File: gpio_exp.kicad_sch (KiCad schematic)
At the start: 17 parts, among them U41 PCA9539AHF

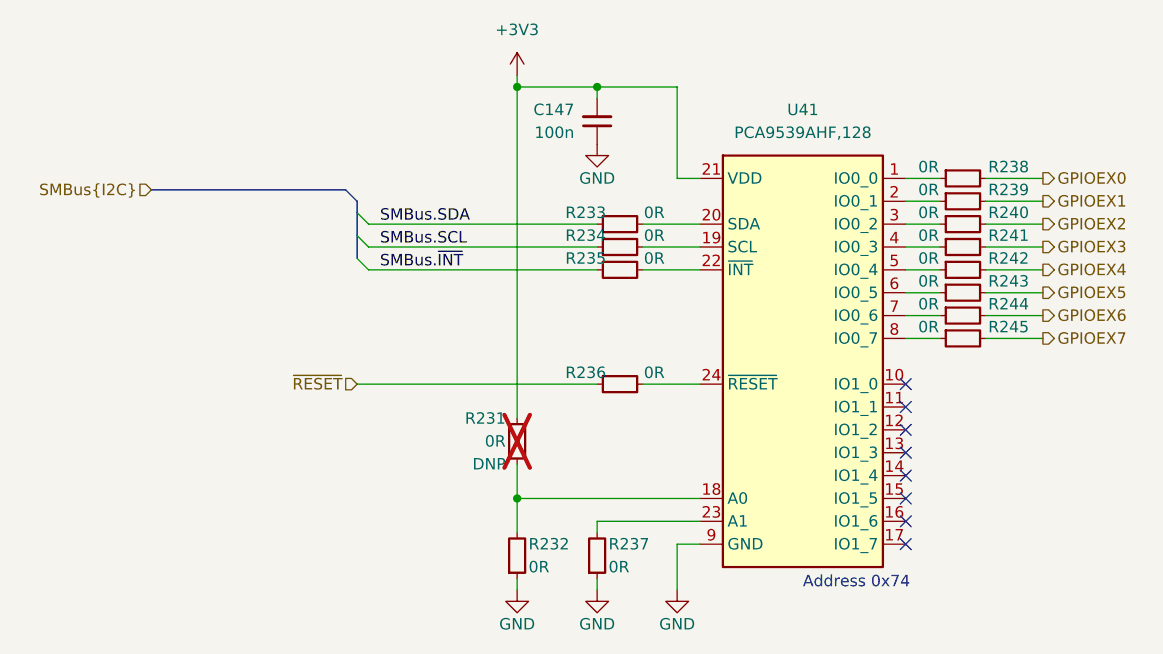
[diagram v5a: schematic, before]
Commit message: Update components from the library
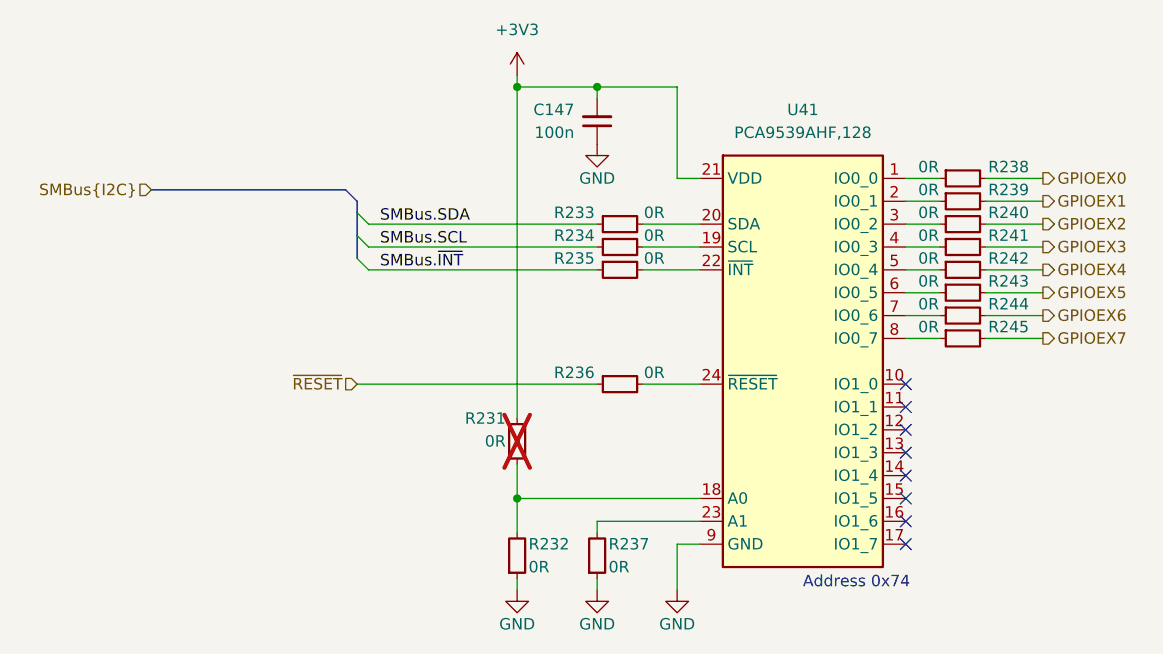
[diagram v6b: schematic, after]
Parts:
- C147, R232, R233, R234, R235, R236, R237, R238, R239, R240, R241, R242, R243, R244, R245: Public (none) -> False
- R231: DNP DNP -> (none); Public (none) -> False
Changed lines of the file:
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@@
       (effects (font (size 1.27 1.27) (thickness 0.15)) (justify left bottom) hide)
+    )
+    (property "Public" "False" (at 247.65 180.34 0)
+      (effects (font (size 1.27 1.27)) (justify left bottom) hide)
     )
     (pin "1")
@@
       (effects (font (size 1.27 1.27) (thickness 0.15)) (justify left bottom) hide)
     )
+    (property "Public" "False" (at 247.65 170.18 0)
+      (effects (font (size 1.27 1.27)) (justify left bottom) hide)
+    )
     (pin "1")
     (pin "2")
@@
       (effects (font (size 1.27 1.27) (thickness 0.15)) (justify left bottom) hide)
     )
+    (property "Public" "False" (at 247.65 167.64 0)
+      (effects (font (size 1.27 1.27)) (justify left bottom) hide)
+    )
     (pin "1")
     (pin "2")
@@
       (effects (font (size 1.27 1.27) (thickness 0.15)) (justify left bottom) hide)
     )
+    (property "Public" "False" (at 247.65 177.8 0)
+      (effects (font (size 1.27 1.27)) (justify left bottom) hide)
+    )
     (pin "1")
     (pin "2")
@@
   (symbol (lib_id "antmicroResistors0402:R_0R_0402") (at 189.23 154.94 0) (unit 1)
     (in_bom yes) (on_board yes) (dnp no)
-    (property "Reference" "R236" (at 187.96 153.67 0)
+    (property "Reference" "R236" (at 186.69 153.67 0)
       (effects (font (size 1.27 1.27) (thickness 0.15)))
     )
@@
       (effects (font (size 1.27 1.27) (thickness 0.15)) (justify left bottom) hide)
     )
+    (property "Public" "False" (at 209.55 185.42 0)
+      (effects (font (size 1.27 1.27)) (justify left bottom) hide)
+    )
     (pin "1")
     (pin "2")
@@
   (symbol (lib_id "antmicroResistors0402:R_0R_0402") (at 189.23 139.7 0) (unit 1)
     (in_bom yes) (on_board yes) (dnp no)
-    (property "Reference" "R234" (at 187.96 138.43 0)
+    (property "Reference" "R234" (at 186.69 138.43 0)
       (effects (font (size 1.27 1.27) (thickness 0.15)))
     )
@@
       (effects (font (size 1.27 1.27) (thickness 0.15)) (justify left bottom) hide)
     )
+    (property "Public" "False" (at 209.55 170.18 0)
+      (effects (font (size 1.27 1.27)) (justify left bottom) hide)
+    )
     (pin "2")
     (pin "1")
@@
     (property "Current" "1A" (at 247.65 172.72 0)
       (effects (font (size 1.27 1.27) (thickness 0.15)) (justify left bottom) hide)
+    )
+    (property "Public" "False" (at 247.65 172.72 0)
+      (effects (font (size 1.27 1.27)) (justify left bottom) hide)
     )
     (pin "1")
@@
       (effects (font (size 1.27 1.27) (thickness 0.15)) (justify left bottom) hide)
     )
+    (property "Public" "False" (at 219.71 156.21 0)
+      (effects (font (size 1.27 1.27)) (justify left bottom) hide)
+    )
     (pin "2")
     (pin "1")
@@
   (symbol (lib_id "antmicroResistors0402:R_0R_0402") (at 189.23 142.24 0) (unit 1)
     (in_bom yes) (on_board yes) (dnp no)
-    (property "Reference" "R235" (at 187.96 140.97 0)
+    (property "Reference" "R235" (at 186.69 140.97 0)
       (effects (font (size 1.27 1.27) (thickness 0.15)))
     )
@@
       (effects (font (size 1.27 1.27) (thickness 0.15)) (justify left bottom) hide)
     )
+    (property "Public" "False" (at 209.55 172.72 0)
+      (effects (font (size 1.27 1.27)) (justify left bottom) hide)
+    )
     (pin "2")
     (pin "1")
@@
     (property "Current" "1A" (at 247.65 165.1 0)
       (effects (font (size 1.27 1.27) (thickness 0.15)) (justify left bottom) hide)
+    )
+    (property "Public" "False" (at 247.65 165.1 0)
+      (effects (font (size 1.27 1.27)) (justify left bottom) hide)
     )
     (pin "1")
@@
       (effects (font (size 1.27 1.27) (thickness 0.15)) (justify left bottom) hide)
     )
-    (property "Datasheet" "https://www.nxp.com/docs/en/data-sheet/PCA9534.pdf" (at 233.68 147.32 0)
+    (property "Datasheet" "https://www.nxp.com/docs/en/data-sheet/PCA9539A.pdf" (at 233.68 147.32 0)
       (effects (font (size 1.27 1.27) (thickness 0.15)) (justify left bottom) hide)
     )
@@
       (effects (font (size 1.27 1.27) (thickness 0.15)) (justify left bottom) hide)
     )
+    (property "Public" "False" (at 247.65 162.56 0)
+      (effects (font (size 1.27 1.27)) (justify left bottom) hide)
+    )
     (pin "1")
     (pin "2")
@@
       (effects (font (size 1.27 1.27) (thickness 0.15)) (justify left bottom) hide)
     )
-    (property "DNP" "DNP" (at 179.07 163.83 90)
-      (effects (font (size 1.27 1.27)) (justify left))
+    (property "Public" "False" (at 210.82 143.51 0)
+      (effects (font (size 1.27 1.27)) (justify left bottom) hide)
     )
     (pin "2")
@@
     (property "Current" "1A" (at 247.65 175.26 0)
       (effects (font (size 1.27 1.27) (thickness 0.15)) (justify left bottom) hide)
+    )
+    (property "Public" "False" (at 247.65 175.26 0)
+      (effects (font (size 1.27 1.27)) (justify left bottom) hide)
     )
     (pin "1")
@@
       (effects (font (size 1.27 1.27) (thickness 0.15)) (justify left bottom) hide)
     )
+    (property "Public" "False" (at 210.82 156.21 0)
+      (effects (font (size 1.27 1.27)) (justify left bottom) hide)
+    )
     (pin "2")
     (pin "1")
@@
   (symbol (lib_id "antmicroResistors0402:R_0R_0402") (at 189.23 137.16 0) (unit 1)
     (in_bom yes) (on_board yes) (dnp no)
-    (property "Reference" "R233" (at 187.96 135.89 0)
+    (property "Reference" "R233" (at 186.69 135.89 0)
       (effects (font (size 1.27 1.27) (thickness 0.15)))
     )
@@
     (property "Current" "1A" (at 209.55 167.64 0)
       (effects (font (size 1.27 1.27) (thickness 0.15)) (justify left bottom) hide)
+    )
+    (property "Public" "False" (at 209.55 167.64 0)
+      (effects (font (size 1.27 1.27)) (justify left bottom) hide)
     )
     (pin "2")
@@
       (effects (font (size 1.27 1.27)) (justify left bottom) hide)
     )
+    (property "Public" "False" (at 156.21 107.95 0)
+      (effects (font (size 1.27 1.27)) (justify left bottom) hide)
+    )
